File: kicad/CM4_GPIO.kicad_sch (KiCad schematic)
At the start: 46 parts, among them J12 nRpiBoot, J13 Conn_01x03, J14 Conn_01x03, J15 AudioOUT, J16 Micro_SD_Card_Det, J17 THD-20-R, J18 GLOBAL_EN, J19 AudioAMP, J9 THD-02-R, U1 TPD4EUSB30, U10 74LVC1G07SE-7, U11 RT9742GGJ5, U2 TPD4EUSB30, U3 MagJack-A70-112-331N126, U8 74LVC1G07SE-7, U9 NC7WZ16

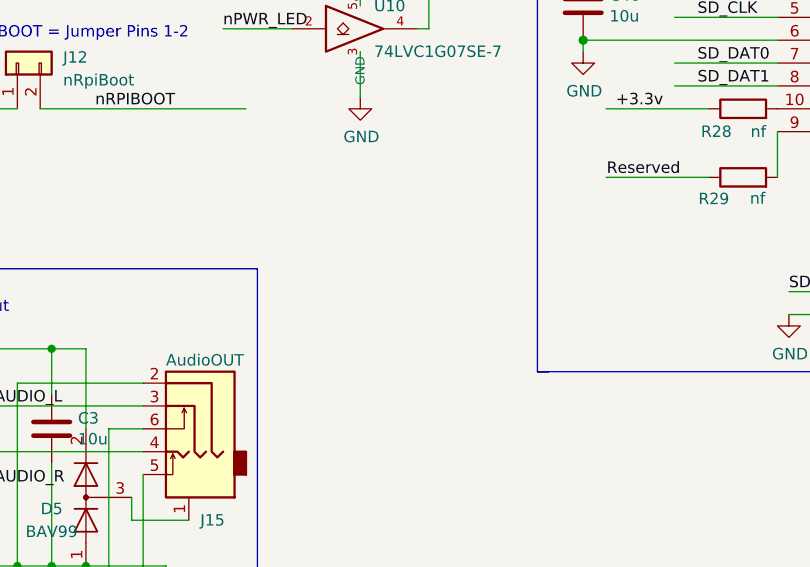
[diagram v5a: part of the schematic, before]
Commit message: Adding I2S MIC connector
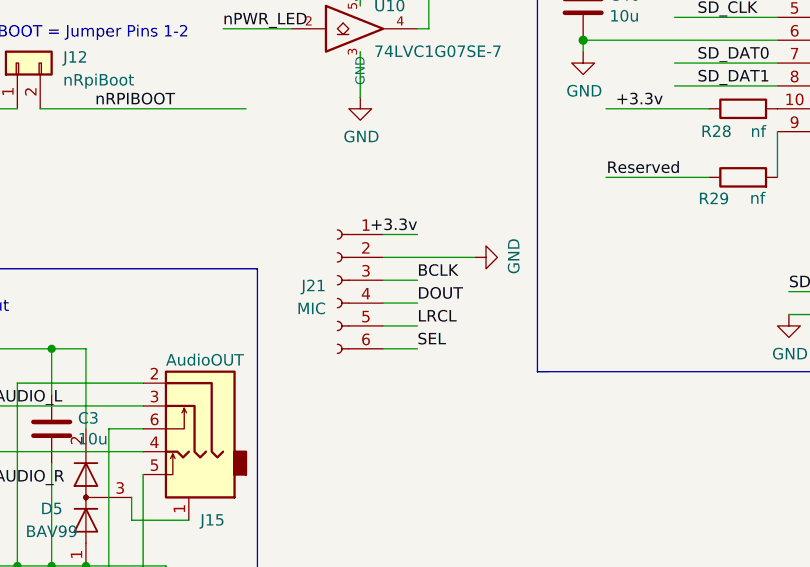
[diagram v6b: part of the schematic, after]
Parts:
- added J21: MIC, Connector_PinSocket_2.54mm:PinSocket_1x06_P2.54mm_Vertical, symbol Connector:Conn_01x06_Female
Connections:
- net +3.3v: now also J21.1 (Pin_1)
- net GND: now also J21.2 (Pin_2)
- new net BCLK: J21.3 (Pin_3)
- new net DOUT: J21.4 (Pin_4)
- new net LRCL: J21.5 (Pin_5)
- new net SEL: J21.6 (Pin_6)
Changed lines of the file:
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@@
     (stroke (width 0) (type solid))
   )
+  (wire (pts (xy 187.96 158.75) (xy 191.77 158.75))
+    (stroke (width 0) (type default))
+  )
   (wire (pts (xy 151.13 173.99) (xy 151.13 185.42))
     (stroke (width 0) (type default))
@@
     (stroke (width 0) (type solid))
   )
+  (wire (pts (xy 187.96 151.13) (xy 198.12 151.13))
+    (stroke (width 0) (type default))
+  )
   (wire (pts (xy 231.775 132.08) (xy 220.345 132.08))
     (stroke (width 0) (type solid))
@@
     (stroke (width 0) (type solid))
   )
+  (wire (pts (xy 187.96 153.67) (xy 191.77 153.67))
+    (stroke (width 0) (type default))
+  )
   (wire (pts (xy 241.935 154.94) (xy 240.665 154.94))
     (stroke (width 0) (type solid))
@@
     (stroke (width 0) (type solid))
   )
+  (wire (pts (xy 187.96 148.59) (xy 191.77 148.59))
+    (stroke (width 0) (type default))
+  )
   (wire (pts (xy 151.13 161.29) (xy 154.94 161.29))
     (stroke (width 0) (type default))
@@
     (stroke (width 0) (type solid))
   )
+  (wire (pts (xy 187.96 156.21) (xy 191.77 156.21))
+    (stroke (width 0) (type default))
+  )
   (wire (pts (xy 152.4 110.49) (xy 170.18 110.49))
     (stroke (width 0) (type solid))
@@
     (stroke (width 0) (type solid))
   )
+  (wire (pts (xy 187.96 161.29) (xy 191.77 161.29))
+    (stroke (width 0) (type default))
+  )
   (wire (pts (xy 36.576 181.61) (xy 49.276 181.61))
     (stroke (width 0) (type default))
@@
     (effects (font (size 1.27 1.27)) (justify left bottom))
   )
+  (label "DOUT" (at 191.77 156.21 0) (fields_autoplaced)
+    (effects (font (size 1.27 1.27)) (justify left bottom))
+  )
   (label "GPIO8" (at 173.99 53.34 0) (fields_autoplaced)
     (effects (font (size 1.27 1.27)) (justify right bottom))
@@
     (effects (font (size 1.27 1.27)) (justify right bottom))
   )
+  (label "+3.3v" (at 191.77 148.59 0) (fields_autoplaced)
+    (effects (font (size 1.27 1.27)) (justify right bottom))
+  )
   (label "GPIO25" (at 175.26 50.8 0) (fields_autoplaced)
     (effects (font (size 1.27 1.27)) (justify right bottom))
@@
     (effects (font (size 1.27 1.27)) (justify right bottom))
   )
+  (label "BCLK" (at 191.77 153.67 0) (fields_autoplaced)
+    (effects (font (size 1.27 1.27)) (justify left bottom))
+  )
   (label "SD_DAT3" (at 111.506 95.25 0) (fields_autoplaced)
     (effects (font (size 1.27 1.27)) (justify right bottom))
@@
     (effects (font (size 1.27 1.27)) (justify right bottom))
   )
+  (label "SEL" (at 191.77 161.29 0) (fields_autoplaced)
+    (effects (font (size 1.27 1.27)) (justify left bottom))
+  )
   (label "nPWR_LED" (at 170.18 125.73 0) (fields_autoplaced)
     (effects (font (size 1.27 1.27)) (justify left bottom))
@@
     (effects (font (size 1.27 1.27)) (justify right bottom))
   )
+  (label "LRCL" (at 191.77 158.75 0) (fields_autoplaced)
+    (effects (font (size 1.27 1.27)) (justify left bottom))
+  )
   (label "GPIO14" (at 110.236 87.63 0) (fields_autoplaced)
     (effects (font (size 1.27 1.27)) (justify right bottom))
@@
     )
   )
+  (symbol (lib_id "Connector:Conn_01x06_Female") (at 182.88 153.67 0) (mirror y) (unit 1)
+    (in_bom yes) (on_board yes) (dnp no)
+    (property "Reference" "J21" (at 181.61 154.305 0)
+      (effects (font (size 1.27 1.27)) (justify left))
+    )
+    (property "Value" "MIC" (at 181.61 156.845 0)
+      (effects (font (size 1.27 1.27)) (justify left))
+    )
+    (property "Footprint" "Connector_PinSocket_2.54mm:PinSocket_1x06_P2.54mm_Vertical" (at 182.88 153.67 0)
+      (effects (font (size 1.27 1.27)) hide)
+    )
+    (property "Datasheet" "~" (at 182.88 153.67 0)
+      (effects (font (size 1.27 1.27)) hide)
+    )
+    (pin "1")
+    (pin "2")
+    (pin "3")
+    (pin "4")
+    (pin "5")
+    (pin "6")
+    (instances
+      (project "Unifying"
+        (path "/9bdfb27f-c9ad-4974-8286-b25e5ffa2770/00000000-0000-0000-0000-00005cff706a"
+          (reference "J21") (unit 1) (value "MIC") (footprint "Connector_PinSocket_2.54mm:PinSocket_1x06_P2.54mm_Vertical")
+        )
+      )
+    )
+  )
   (symbol (lib_id "Device:C") (at 135.89 176.53 90) (unit 1)
     (in_bom yes) (on_board yes) (dnp no)
@@
         )
       )
+    )
+  )
+  (symbol (lib_id "power:GND") (at 198.12 151.13 90) (unit 1)
+    (in_bom yes) (on_board yes) (dnp no)
+    (property "Reference" "#PWR0102" (at 204.47 151.13 0)
+      (effects (font (size 1.27 1.27)) hide)
+    )
+    (property "Value" "GND" (at 202.5142 151.003 0)
+      (effects (font (size 1.27 1.27)))
+    )
+    (property "Footprint" "" (at 198.12 151.13 0)
+      (effects (font (size 1.27 1.27)) hide)
+    )
+    (property "Datasheet" "" (at 198.12 151.13 0)
+      (effects (font (size 1.27 1.27)) hide)
+    )
+    (pin "1")
+    (instances
+      (project "Unifying"
+        (path "/9bdfb27f-c9ad-4974-8286-b25e5ffa2770/00000000-0000-0000-0000-00005cff706a"
+          (reference "#PWR0102") (unit 1) (value "GND") (footprint "")
+        )
+      )

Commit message: Connecting MIC fix #20
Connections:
- net GPIO18 is gone; now on net BCLK: J17.12 (Pin_12), Module1.49 (GPIO18)
- net GPIO20 is gone; now on net DOUT: J17.38 (Pin_38), Module1.27 (GPIO20)
- net LRCL is gone; now on net GPIO19: J21.5 (Pin_5)
- net SEL is gone; now on net GND: J21.6 (Pin_6)
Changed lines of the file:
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@@
     (stroke (width 0) (type solid))
   )
+  (wire (pts (xy 161.29 146.05) (xy 168.91 146.05))
+    (stroke (width 0) (type default))
+  )
   (wire (pts (xy 259.715 146.05) (xy 259.715 154.94))
     (stroke (width 0) (type default))
@@
     (stroke (width 0) (type solid))
   )
+  (wire (pts (xy 161.29 148.59) (xy 168.91 148.59))
+    (stroke (width 0) (type default))
+  )
   (wire (pts (xy 220.345 129.54) (xy 231.775 129.54))
     (stroke (width 0) (type solid))
@@
     (stroke (width 0) (type solid))
   )
+  (wire (pts (xy 161.29 143.51) (xy 168.91 143.51))
+    (stroke (width 0) (type default))
+  )
   (wire (pts (xy 39.116 140.97) (xy 37.846 140.97))
     (stroke (width 0) (type solid))
@@
     (stroke (width 0) (type default))
   )
+  (wire (pts (xy 161.29 140.97) (xy 168.91 140.97))
+    (stroke (width 0) (type default))
+  )
   (wire (pts (xy 210.185 127) (xy 231.775 127))
     (stroke (width 0) (type solid))
@@
     (effects (font (size 1.27 1.27)) (justify right bottom))
   )
+  (label "GPIO19" (at 161.29 146.05 0) (fields_autoplaced)
+    (effects (font (size 1.27 1.27)) (justify right bottom))
+  )
   (label "GPIO27" (at 32.766 77.47 0) (fields_autoplaced)
     (effects (font (size 1.27 1.27)) (justify right bottom))
@@
     (effects (font (size 1.27 1.27)) (justify left bottom))
   )
+  (label "LRCL" (at 168.91 146.05 0) (fields_autoplaced)
+    (effects (font (size 1.27 1.27)) (justify left bottom))
+  )
   (label "BT_nDis" (at 112.6236 133.35 0) (fields_autoplaced)
     (effects (font (size 1.27 1.27)) (justify right bottom))
@@
     (effects (font (size 1.27 1.27)) (justify left bottom))
   )
+  (label "DOUT" (at 168.91 143.51 0) (fields_autoplaced)
+    (effects (font (size 1.27 1.27)) (justify left bottom))
+  )
   (label "GPIO17" (at 32.766 80.01 0) (fields_autoplaced)
     (effects (font (size 1.27 1.27)) (justify right bottom))
@@
     (effects (font (size 1.27 1.27)) (justify left bottom))
   )
+  (label "GPIO20" (at 161.29 143.51 0) (fields_autoplaced)
+    (effects (font (size 1.27 1.27)) (justify right bottom))
+  )
   (label "SD_DAT3" (at 111.506 95.25 0) (fields_autoplaced)
     (effects (font (size 1.27 1.27)) (justify right bottom))
@@
     (effects (font (size 1.27 1.27)) (justify right bottom))
   )
+  (label "BCLK" (at 168.91 140.97 0) (fields_autoplaced)
+    (effects (font (size 1.27 1.27)) (justify left bottom))
+  )
   (label "GPIO15" (at 175.26 35.56 0) (fields_autoplaced)
     (effects (font (size 1.27 1.27)) (justify right bottom))
@@
     (effects (font (size 1.27 1.27)) (justify right bottom))
   )
+  (label "GPIO18" (at 161.29 140.97 0) (fields_autoplaced)
+    (effects (font (size 1.27 1.27)) (justify right bottom))
+  )
   (label "GPIO11" (at 32.766 64.77 0) (fields_autoplaced)
     (effects (font (size 1.27 1.27)) (justify right bottom))
@@
     (effects (font (size 1.27 1.27)) (justify right bottom))
   )
+  (label "SEL" (at 168.91 148.59 0) (fields_autoplaced)
+    (effects (font (size 1.27 1.27)) (justify left bottom))
+  )
   (label "SD_DAT1" (at 222.885 132.08 0) (fields_autoplaced)
     (effects (font (size 1.27 1.27)) (justify left bottom))
@@
         )
       )
+    )
+  )
+  (symbol (lib_id "power:GND") (at 161.29 148.59 270) (unit 1)
+    (in_bom yes) (on_board yes) (dnp no)
+    (property "Reference" "#PWR046" (at 154.94 148.59 0)
+      (effects (font (size 1.27 1.27)) hide)
+    )
+    (property "Value" "GND" (at 156.8958 148.717 0)
+      (effects (font (size 1.27 1.27)))
+    )
+    (property "Footprint" "" (at 161.29 148.59 0)
+      (effects (font (size 1.27 1.27)) hide)
+    )
+    (property "Datasheet" "" (at 161.29 148.59 0)
+      (effects (font (size 1.27 1.27)) hide)
+    )
+    (pin "1")
+    (instances
+      (project "Unifying"
+        (path "/9bdfb27f-c9ad-4974-8286-b25e5ffa2770/00000000-0000-0000-0000-00005cff706a"
+          (reference "#PWR046") (unit 1) (value "GND") (footprint "")
+        )
+      )
